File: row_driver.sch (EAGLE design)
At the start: 27 parts, among them IC1 74HC138N, Q1 BC327, Q2 BC327, Q3 BC327, Q4 BC327, Q5 BC327, Q6 BC327, Q7 BC327, Q8 BC327

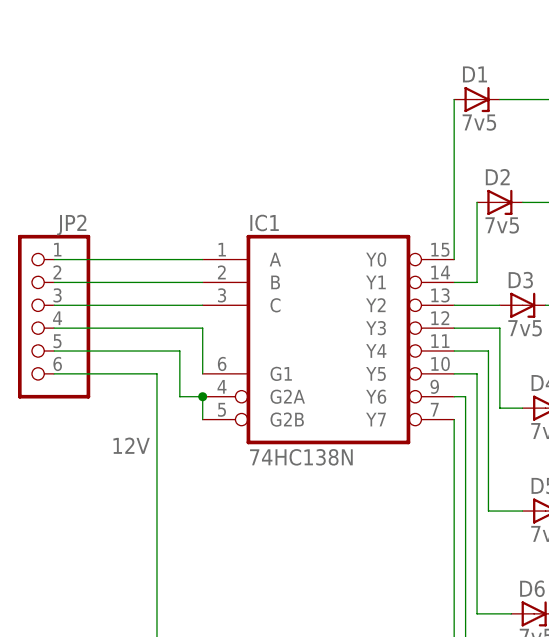
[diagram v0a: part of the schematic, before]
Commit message: row_driver: added GND and VCC
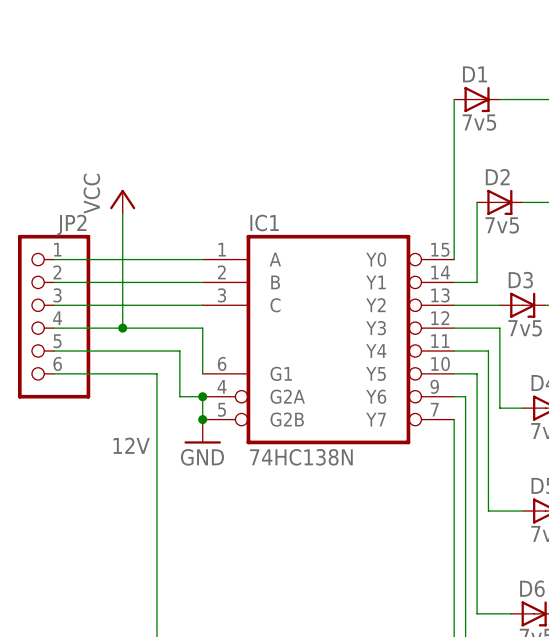
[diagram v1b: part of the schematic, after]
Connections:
- net N$6 renamed VCC
- net N$7 renamed GND
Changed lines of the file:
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@@
 <part name="R7" library="resistor" deviceset="R-EU_" device="0207/12" value="1k"/>
 <part name="R8" library="resistor" deviceset="R-EU_" device="0207/12" value="1k"/>
+<part name="P+1" library="supply1" deviceset="VCC" device=""/>
+<part name="GND1" library="supply1" deviceset="GND" device=""/>
 </parts>
 <sheets>
@@
 <instance part="R7" gate="G$1" x="69.85" y="58.42"/>
 <instance part="R8" gate="G$1" x="69.85" y="46.99"/>
+<instance part="P+1" gate="VCC" x="12.7" y="116.84"/>
+<instance part="GND1" gate="1" x="21.59" y="88.9"/>
 </instances>
 <busses>
@@
 <pinref part="IC1" gate="A" pin="C"/>
 <wire x1="5.08" y1="104.14" x2="21.59" y2="104.14" width="0.1524" layer="91"/>
-</segment>
-</net>
-<net name="N$6" class="0">
-<segment>
-<pinref part="JP2" gate="A" pin="4"/>
-<pinref part="IC1" gate="A" pin="G1"/>
-<wire x1="5.08" y1="101.6" x2="21.59" y2="101.6" width="0.1524" layer="91"/>
-<wire x1="21.59" y1="101.6" x2="21.59" y2="96.52" width="0.1524" layer="91"/>
-</segment>
-</net>
-<net name="N$7" class="0">
-<segment>
-<pinref part="IC1" gate="A" pin="G2B"/>
-<pinref part="IC1" gate="A" pin="G2A"/>
-<wire x1="21.59" y1="91.44" x2="21.59" y2="93.98" width="0.1524" layer="91"/>
-<wire x1="21.59" y1="93.98" x2="19.05" y2="93.98" width="0.1524" layer="91"/>
-<wire x1="19.05" y1="93.98" x2="19.05" y2="99.06" width="0.1524" layer="91"/>
-<pinref part="JP2" gate="A" pin="5"/>
-<wire x1="19.05" y1="99.06" x2="5.08" y2="99.06" width="0.1524" layer="91"/>
-<junction x="21.59" y="93.98"/>
 </segment>
 </net>
@@
 </segment>
 </net>
+<net name="VCC" class="0">
+<segment>
+<pinref part="JP2" gate="A" pin="4"/>
+<pinref part="IC1" gate="A" pin="G1"/>
+<wire x1="5.08" y1="101.6" x2="12.7" y2="101.6" width="0.1524" layer="91"/>
+<wire x1="12.7" y1="101.6" x2="21.59" y2="101.6" width="0.1524" layer="91"/>
+<wire x1="21.59" y1="101.6" x2="21.59" y2="96.52" width="0.1524" layer="91"/>
+<pinref part="P+1" gate="VCC" pin="VCC"/>
+<wire x1="12.7" y1="114.3" x2="12.7" y2="101.6" width="0.1524" layer="91"/>
+<junction x="12.7" y="101.6"/>
+</segment>
+</net>
+<net name="GND" class="0">
+<segment>
+<pinref part="IC1" gate="A" pin="G2B"/>
+<pinref part="IC1" gate="A" pin="G2A"/>
+<wire x1="21.59" y1="91.44" x2="21.59" y2="93.98" width="0.1524" layer="91"/>
+<wire x1="21.59" y1="93.98" x2="19.05" y2="93.98" width="0.1524" layer="91"/>
+<wire x1="19.05" y1="93.98" x2="19.05" y2="99.06" width="0.1524" layer="91"/>
+<pinref part="JP2" gate="A" pin="5"/>
+<wire x1="19.05" y1="99.06" x2="5.08" y2="99.06" width="0.1524" layer="91"/>
+<junction x="21.59" y="93.98"/>
+<pinref part="GND1" gate="1" pin="GND"/>
+<junction x="21.59" y="91.44"/>
+</segment>
+</net>
